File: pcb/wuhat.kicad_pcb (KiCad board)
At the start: 2 copper layers, 65 x 30 mm, 44 parts, among them J1 GPIOcon, U1 MCP3002, U3 ID

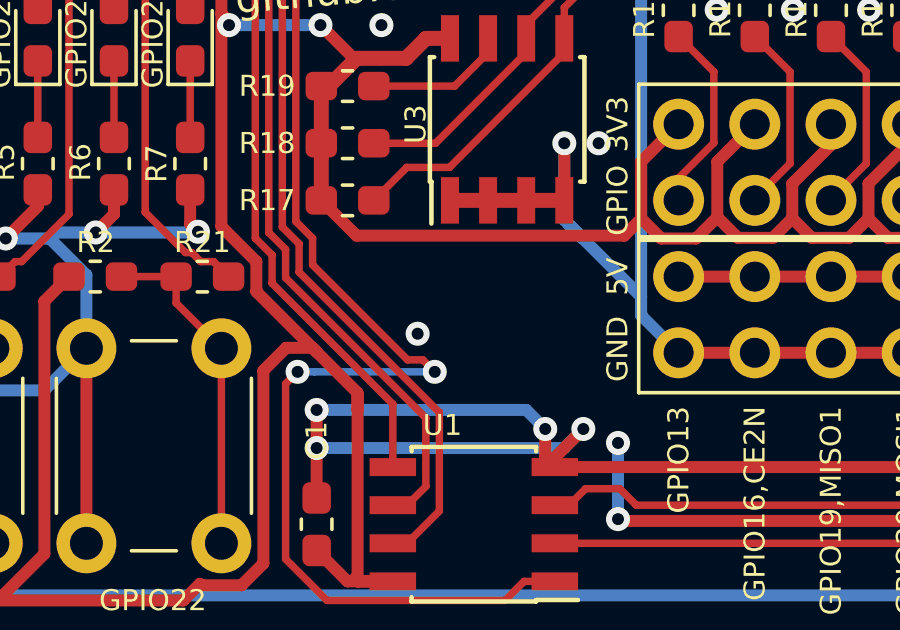
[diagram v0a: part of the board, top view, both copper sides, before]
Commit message: added revision string to pcb
bumped the revision to 7E4.0 (hex for 2020.0).
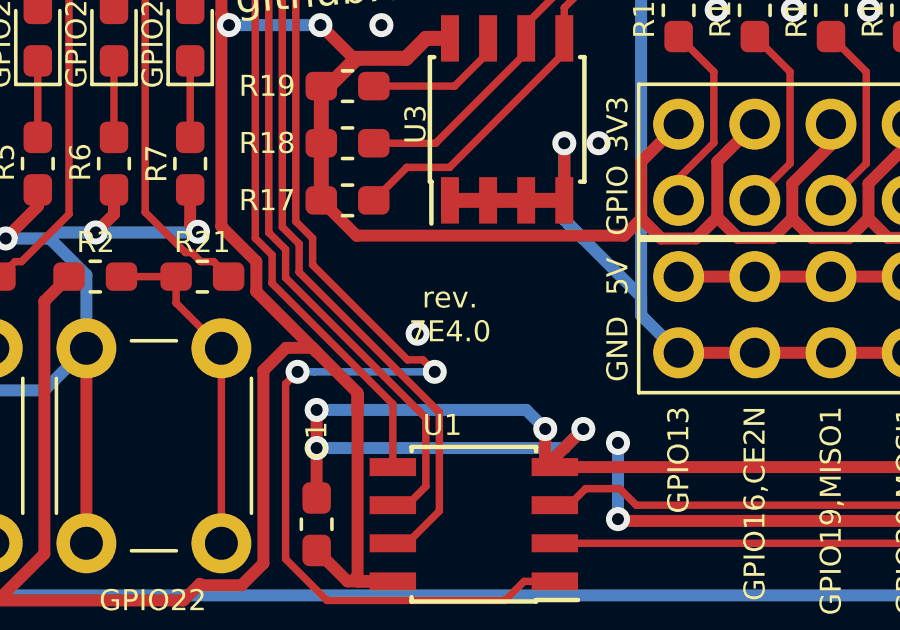
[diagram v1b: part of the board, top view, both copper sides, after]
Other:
- board text added: "rev. 7E4.0"
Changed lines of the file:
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@@
-(kicad_pcb (version 20171130) (host pcbnew 5.0.1+dfsg1-3~bpo9+1)
+(kicad_pcb (version 20171130) (host pcbnew "(5.1.4)-1")
   (general
     (thickness 1.6)
-    (drawings 43)
+    (drawings 44)
     (tracks 509)
     (zones 0)
@@
     (title WUhat)
     (date 2018-12-03)
-    (rev 0.1)
+    (rev 7E4.0)
   )
   (layers
-    (0 F.Cu signal)
-    (31 B.Cu signal)
+    (0 F.Cu signal hide)
+    (31 B.Cu signal hide)
     (32 B.Adhes user hide)
     (33 F.Adhes user hide)
@@
     (zone_45_only no)
     (trace_min 0.2)
-    (segment_width 0.15)
-    (edge_width 0.15)
     (via_size 0.8)
     (via_drill 0.4)
@@
     (uvia_min_size 0.2)
     (uvia_min_drill 0.1)
+    (edge_width 0.15)
+    (segment_width 0.15)
     (pcb_text_width 0.3)
     (pcb_text_size 1.5 1.5)
@@
     (aux_axis_origin 134.1 99.23)
     (grid_origin 134.1 99.23)
-    (visible_elements FFFFFF7F)
+    (visible_elements 7FFFFFFF)
     (pcbplotparams
       (layerselection 0x010f0_ffffffff)
@@
     (pad "" np_thru_hole circle (at 0 0) (size 6.2 6.2) (drill 2.75) (layers *.Cu *.Mask))
   )
+  (gr_text "rev.\n7E4.0" (at 137.91 114.47) (layer F.SilkS)
+    (effects (font (size 0.7 0.7) (thickness 0.15)))
+  )
   (gr_text https://github.com/wuhat (at 135.878 103.1035) (layer B.SilkS)

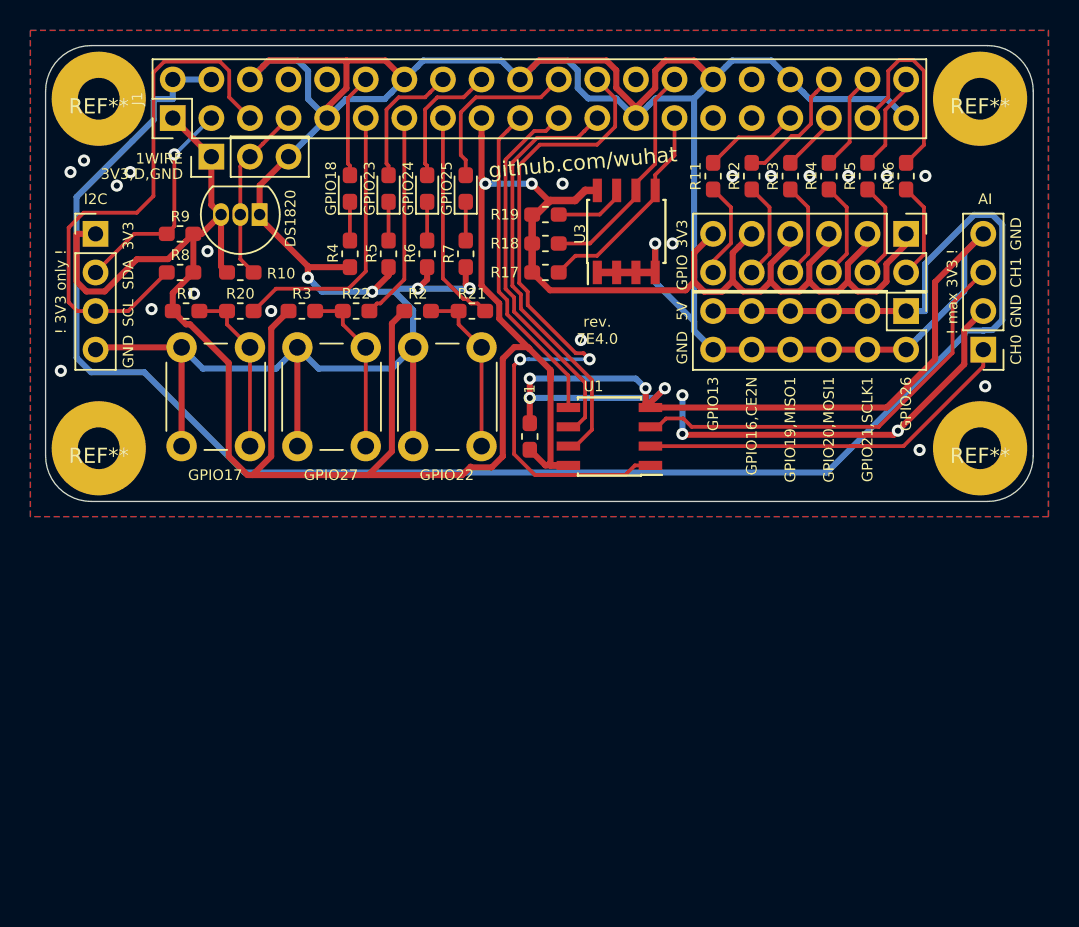
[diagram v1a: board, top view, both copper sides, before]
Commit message: expanded board to full size hat
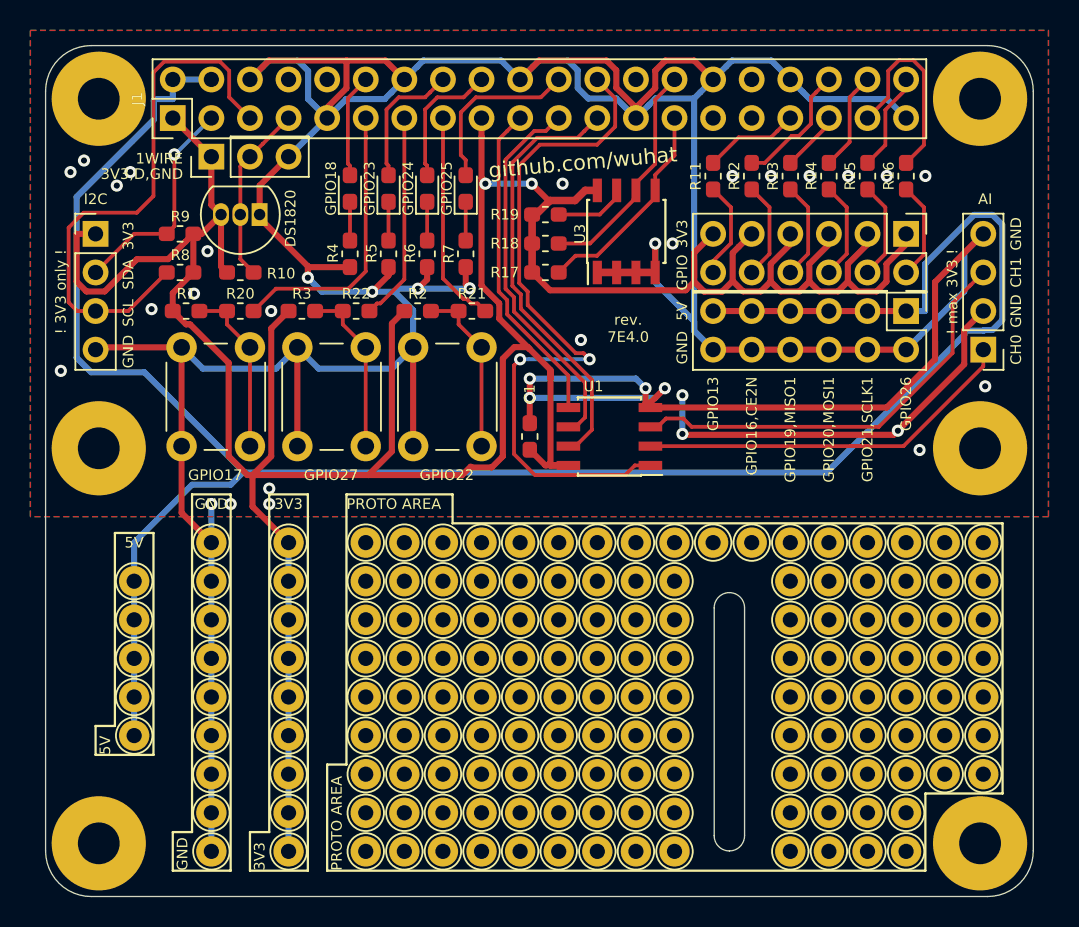
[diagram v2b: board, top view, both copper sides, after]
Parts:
- added REF**: TestPoint_THTPad_D2.0mm_Drill1.0mm, TestPoint:TestPoint_THTPad_D2.0mm_Drill1.0mm, F.Cu at (112.5, 148.8)
- added REF**: TestPoint_THTPad_D2.0mm_Drill1.0mm, TestPoint:TestPoint_THTPad_D2.0mm_Drill1.0mm, F.Cu at (117.6, 138.6)
- added REF**: TestPoint_THTPad_D2.0mm_Drill1.0mm, TestPoint:TestPoint_THTPad_D2.0mm_Drill1.0mm, F.Cu at (143.0, 146.2)
- added REF**: TestPoint_THTPad_D2.0mm_Drill1.0mm, TestPoint:TestPoint_THTPad_D2.0mm_Drill1.0mm, F.Cu at (143.0, 138.6)
- added REF**: TestPoint_THTPad_D2.0mm_Drill1.0mm, TestPoint:TestPoint_THTPad_D2.0mm_Drill1.0mm, F.Cu at (163.3, 143.7)
- added REF**: TestPoint_THTPad_D2.0mm_Drill1.0mm, TestPoint:TestPoint_THTPad_D2.0mm_Drill1.0mm, F.Cu at (160.8, 143.7)
- added REF**: TestPoint_THTPad_D2.0mm_Drill1.0mm, TestPoint:TestPoint_THTPad_D2.0mm_Drill1.0mm, F.Cu at (163.3, 138.6)
- added REF**: TestPoint_THTPad_D2.0mm_Drill1.0mm, TestPoint:TestPoint_THTPad_D2.0mm_Drill1.0mm, F.Cu at (163.3, 141.1)
- added REF**: TestPoint_THTPad_D2.0mm_Drill1.0mm, TestPoint:TestPoint_THTPad_D2.0mm_Drill1.0mm, F.Cu at (163.3, 128.4)
- added REF**: TestPoint_THTPad_D2.0mm_Drill1.0mm, TestPoint:TestPoint_THTPad_D2.0mm_Drill1.0mm, F.Cu at (163.3, 133.5)
- added REF**: TestPoint_THTPad_D2.0mm_Drill1.0mm, TestPoint:TestPoint_THTPad_D2.0mm_Drill1.0mm, F.Cu at (163.3, 136.1)
- added REF**: TestPoint_THTPad_D2.0mm_Drill1.0mm, TestPoint:TestPoint_THTPad_D2.0mm_Drill1.0mm, F.Cu at (163.3, 131.0)
- added REF**: TestPoint_THTPad_D2.0mm_Drill1.0mm, TestPoint:TestPoint_THTPad_D2.0mm_Drill1.0mm, F.Cu at (112.5, 136.1)
- added REF**: TestPoint_THTPad_D2.0mm_Drill1.0mm, TestPoint:TestPoint_THTPad_D2.0mm_Drill1.0mm, F.Cu at (160.8, 138.6)
- added REF**: TestPoint_THTPad_D2.0mm_Drill1.0mm, TestPoint:TestPoint_THTPad_D2.0mm_Drill1.0mm, F.Cu at (160.8, 141.1)
- added REF**: TestPoint_THTPad_D2.0mm_Drill1.0mm, TestPoint:TestPoint_THTPad_D2.0mm_Drill1.0mm, F.Cu at (160.8, 133.5)
- added REF**: TestPoint_THTPad_D2.0mm_Drill1.0mm, TestPoint:TestPoint_THTPad_D2.0mm_Drill1.0mm, F.Cu at (160.8, 136.1)
- added REF**: TestPoint_THTPad_D2.0mm_Drill1.0mm, TestPoint:TestPoint_THTPad_D2.0mm_Drill1.0mm, F.Cu at (160.8, 128.4)
- added REF**: TestPoint_THTPad_D2.0mm_Drill1.0mm, TestPoint:TestPoint_THTPad_D2.0mm_Drill1.0mm, F.Cu at (160.8, 131.0)
- added REF**: TestPoint_THTPad_D2.0mm_Drill1.0mm, TestPoint:TestPoint_THTPad_D2.0mm_Drill1.0mm, F.Cu at (137.9, 128.4)
- added REF**: TestPoint_THTPad_D2.0mm_Drill1.0mm, TestPoint:TestPoint_THTPad_D2.0mm_Drill1.0mm, F.Cu at (140.4, 128.4)
- added REF**: TestPoint_THTPad_D2.0mm_Drill1.0mm, TestPoint:TestPoint_THTPad_D2.0mm_Drill1.0mm, F.Cu at (143.0, 128.4)
- added REF**: TestPoint_THTPad_D2.0mm_Drill1.0mm, TestPoint:TestPoint_THTPad_D2.0mm_Drill1.0mm, F.Cu at (145.5, 128.4)
- added REF**: TestPoint_THTPad_D2.0mm_Drill1.0mm, TestPoint:TestPoint_THTPad_D2.0mm_Drill1.0mm, F.Cu at (117.6, 136.1)
- added REF**: TestPoint_THTPad_D2.0mm_Drill1.0mm, TestPoint:TestPoint_THTPad_D2.0mm_Drill1.0mm, F.Cu at (153.2, 128.4)
- added REF**: TestPoint_THTPad_D2.0mm_Drill1.0mm, TestPoint:TestPoint_THTPad_D2.0mm_Drill1.0mm, F.Cu at (155.7, 128.4)
- added REF**: TestPoint_THTPad_D2.0mm_Drill1.0mm, TestPoint:TestPoint_THTPad_D2.0mm_Drill1.0mm, F.Cu at (148.1, 128.4)
- added REF**: TestPoint_THTPad_D2.0mm_Drill1.0mm, TestPoint:TestPoint_THTPad_D2.0mm_Drill1.0mm, F.Cu at (150.6, 128.4)
- added REF**: TestPoint_THTPad_D2.0mm_Drill1.0mm, TestPoint:TestPoint_THTPad_D2.0mm_Drill1.0mm, F.Cu at (150.6, 133.5)
- added REF**: TestPoint_THTPad_D2.0mm_Drill1.0mm, TestPoint:TestPoint_THTPad_D2.0mm_Drill1.0mm, F.Cu at (150.6, 143.7)
- added REF**: TestPoint_THTPad_D2.0mm_Drill1.0mm, TestPoint:TestPoint_THTPad_D2.0mm_Drill1.0mm, F.Cu at (150.6, 136.1)
- added REF**: TestPoint_THTPad_D2.0mm_Drill1.0mm, TestPoint:TestPoint_THTPad_D2.0mm_Drill1.0mm, F.Cu at (150.6, 146.2)
- added REF**: TestPoint_THTPad_D2.0mm_Drill1.0mm, TestPoint:TestPoint_THTPad_D2.0mm_Drill1.0mm, F.Cu at (150.6, 138.6)
- added REF**: TestPoint_THTPad_D2.0mm_Drill1.0mm, TestPoint:TestPoint_THTPad_D2.0mm_Drill1.0mm, F.Cu at (150.6, 148.8)
- added REF**: TestPoint_THTPad_D2.0mm_Drill1.0mm, TestPoint:TestPoint_THTPad_D2.0mm_Drill1.0mm, F.Cu at (112.5, 133.5)
- added REF**: TestPoint_THTPad_D2.0mm_Drill1.0mm, TestPoint:TestPoint_THTPad_D2.0mm_Drill1.0mm, F.Cu at (150.6, 131.0)
- added REF**: TestPoint_THTPad_D2.0mm_Drill1.0mm, TestPoint:TestPoint_THTPad_D2.0mm_Drill1.0mm, F.Cu at (150.6, 141.1)
- added REF**: TestPoint_THTPad_D2.0mm_Drill1.0mm, TestPoint:TestPoint_THTPad_D2.0mm_Drill1.0mm, F.Cu at (153.2, 146.2)
- added REF**: TestPoint_THTPad_D2.0mm_Drill1.0mm, TestPoint:TestPoint_THTPad_D2.0mm_Drill1.0mm, F.Cu at (153.2, 143.7)
- added REF**: TestPoint_THTPad_D2.0mm_Drill1.0mm, TestPoint:TestPoint_THTPad_D2.0mm_Drill1.0mm, F.Cu at (153.2, 136.1)
- added REF**: TestPoint_THTPad_D2.0mm_Drill1.0mm, TestPoint:TestPoint_THTPad_D2.0mm_Drill1.0mm, F.Cu at (153.2, 138.6)
- added REF**: TestPoint_THTPad_D2.0mm_Drill1.0mm, TestPoint:TestPoint_THTPad_D2.0mm_Drill1.0mm, F.Cu at (153.2, 131.0)
- added REF**: TestPoint_THTPad_D2.0mm_Drill1.0mm, TestPoint:TestPoint_THTPad_D2.0mm_Drill1.0mm, F.Cu at (153.2, 133.5)
- added REF**: TestPoint_THTPad_D2.0mm_Drill1.0mm, TestPoint:TestPoint_THTPad_D2.0mm_Drill1.0mm, F.Cu at (153.2, 141.1)
- added REF**: TestPoint_THTPad_D2.0mm_Drill1.0mm, TestPoint:TestPoint_THTPad_D2.0mm_Drill1.0mm, F.Cu at (153.2, 148.8)
- added REF**: TestPoint_THTPad_D2.0mm_Drill1.0mm, TestPoint:TestPoint_THTPad_D2.0mm_Drill1.0mm, F.Cu at (117.6, 133.5)
- added REF**: TestPoint_THTPad_D2.0mm_Drill1.0mm, TestPoint:TestPoint_THTPad_D2.0mm_Drill1.0mm, F.Cu at (155.7, 148.8)
- added REF**: TestPoint_THTPad_D2.0mm_Drill1.0mm, TestPoint:TestPoint_THTPad_D2.0mm_Drill1.0mm, F.Cu at (155.7, 146.2)
- added REF**: TestPoint_THTPad_D2.0mm_Drill1.0mm, TestPoint:TestPoint_THTPad_D2.0mm_Drill1.0mm, F.Cu at (155.7, 141.1)
- added REF**: TestPoint_THTPad_D2.0mm_Drill1.0mm, TestPoint:TestPoint_THTPad_D2.0mm_Drill1.0mm, F.Cu at (155.7, 143.7)
- added REF**: TestPoint_THTPad_D2.0mm_Drill1.0mm, TestPoint:TestPoint_THTPad_D2.0mm_Drill1.0mm, F.Cu at (155.7, 136.1)
- added REF**: TestPoint_THTPad_D2.0mm_Drill1.0mm, TestPoint:TestPoint_THTPad_D2.0mm_Drill1.0mm, F.Cu at (155.7, 138.6)
- added REF**: TestPoint_THTPad_D2.0mm_Drill1.0mm, TestPoint:TestPoint_THTPad_D2.0mm_Drill1.0mm, F.Cu at (155.7, 131.0)
- added REF**: TestPoint_THTPad_D2.0mm_Drill1.0mm, TestPoint:TestPoint_THTPad_D2.0mm_Drill1.0mm, F.Cu at (155.7, 133.5)
- added REF**: TestPoint_THTPad_D2.0mm_Drill1.0mm, TestPoint:TestPoint_THTPad_D2.0mm_Drill1.0mm, F.Cu at (158.2, 148.8)
- added REF**: TestPoint_THTPad_D2.0mm_Drill1.0mm, TestPoint:TestPoint_THTPad_D2.0mm_Drill1.0mm, F.Cu at (158.2, 146.2)
- added REF**: TestPoint_THTPad_D2.0mm_Drill1.0mm, TestPoint:TestPoint_THTPad_D2.0mm_Drill1.0mm, F.Cu at (117.6, 131.0)
- added REF**: TestPoint_THTPad_D2.0mm_Drill1.0mm, TestPoint:TestPoint_THTPad_D2.0mm_Drill1.0mm, F.Cu at (158.2, 143.7)
- added REF**: TestPoint_THTPad_D2.0mm_Drill1.0mm, TestPoint:TestPoint_THTPad_D2.0mm_Drill1.0mm, F.Cu at (158.2, 141.1)
- added REF**: TestPoint_THTPad_D2.0mm_Drill1.0mm, TestPoint:TestPoint_THTPad_D2.0mm_Drill1.0mm, F.Cu at (158.2, 138.6)
- added REF**: TestPoint_THTPad_D2.0mm_Drill1.0mm, TestPoint:TestPoint_THTPad_D2.0mm_Drill1.0mm, F.Cu at (158.2, 133.5)
- added REF**: TestPoint_THTPad_D2.0mm_Drill1.0mm, TestPoint:TestPoint_THTPad_D2.0mm_Drill1.0mm, F.Cu at (158.2, 136.1)
- added REF**: TestPoint_THTPad_D2.0mm_Drill1.0mm, TestPoint:TestPoint_THTPad_D2.0mm_Drill1.0mm, F.Cu at (158.2, 131.0)
- added REF**: TestPoint_THTPad_D2.0mm_Drill1.0mm, TestPoint:TestPoint_THTPad_D2.0mm_Drill1.0mm, F.Cu at (158.2, 128.4)
- added REF**: mounting_hole, WUhat Artwork:mounting_hole, F.Cu at (163.1, 148.2)
- added REF**: TestPoint_THTPad_D2.0mm_Drill1.0mm, TestPoint:TestPoint_THTPad_D2.0mm_Drill1.0mm, F.Cu at (112.5, 131.0)
- added REF**: TestPoint_THTPad_D2.0mm_Drill1.0mm, TestPoint:TestPoint_THTPad_D2.0mm_Drill1.0mm, F.Cu at (107.4, 141.1)
- added REF**: TestPoint_THTPad_D2.0mm_Drill1.0mm, TestPoint:TestPoint_THTPad_D2.0mm_Drill1.0mm, F.Cu at (107.4, 138.6)
- added REF**: TestPoint_THTPad_D2.0mm_Drill1.0mm, TestPoint:TestPoint_THTPad_D2.0mm_Drill1.0mm, F.Cu at (107.4, 136.1)
- added REF**: TestPoint_THTPad_D2.0mm_Drill1.0mm, TestPoint:TestPoint_THTPad_D2.0mm_Drill1.0mm, F.Cu at (117.6, 148.8)
- added REF**: TestPoint_THTPad_D2.0mm_Drill1.0mm, TestPoint:TestPoint_THTPad_D2.0mm_Drill1.0mm, F.Cu at (107.4, 133.5)
- added REF**: TestPoint_THTPad_D2.0mm_Drill1.0mm, TestPoint:TestPoint_THTPad_D2.0mm_Drill1.0mm, F.Cu at (135.4, 128.4)
- added REF**: TestPoint_THTPad_D2.0mm_Drill1.0mm, TestPoint:TestPoint_THTPad_D2.0mm_Drill1.0mm, F.Cu at (130.3, 128.4)
- added REF**: TestPoint_THTPad_D2.0mm_Drill1.0mm, TestPoint:TestPoint_THTPad_D2.0mm_Drill1.0mm, F.Cu at (125.2, 128.4)
- added REF**: TestPoint_THTPad_D2.0mm_Drill1.0mm, TestPoint:TestPoint_THTPad_D2.0mm_Drill1.0mm, F.Cu at (107.4, 131.0)
- added REF**: TestPoint_THTPad_D2.0mm_Drill1.0mm, TestPoint:TestPoint_THTPad_D2.0mm_Drill1.0mm, F.Cu at (117.6, 128.4)
- added REF**: TestPoint_THTPad_D2.0mm_Drill1.0mm, TestPoint:TestPoint_THTPad_D2.0mm_Drill1.0mm, F.Cu at (112.5, 128.4)
- added REF**: TestPoint_THTPad_D2.0mm_Drill1.0mm, TestPoint:TestPoint_THTPad_D2.0mm_Drill1.0mm, F.Cu at (122.7, 128.4)
- added REF**: TestPoint_THTPad_D2.0mm_Drill1.0mm, TestPoint:TestPoint_THTPad_D2.0mm_Drill1.0mm, F.Cu at (125.2, 131.0)
- added REF**: TestPoint_THTPad_D2.0mm_Drill1.0mm, TestPoint:TestPoint_THTPad_D2.0mm_Drill1.0mm, F.Cu at (122.7, 148.8)
- added REF**: TestPoint_THTPad_D2.0mm_Drill1.0mm, TestPoint:TestPoint_THTPad_D2.0mm_Drill1.0mm, F.Cu at (112.5, 146.2)
- added REF**: TestPoint_THTPad_D2.0mm_Drill1.0mm, TestPoint:TestPoint_THTPad_D2.0mm_Drill1.0mm, F.Cu at (125.2, 146.2)
- added REF**: TestPoint_THTPad_D2.0mm_Drill1.0mm, TestPoint:TestPoint_THTPad_D2.0mm_Drill1.0mm, F.Cu at (125.2, 133.5)
- added REF**: TestPoint_THTPad_D2.0mm_Drill1.0mm, TestPoint:TestPoint_THTPad_D2.0mm_Drill1.0mm, F.Cu at (125.2, 141.1)
- added REF**: TestPoint_THTPad_D2.0mm_Drill1.0mm, TestPoint:TestPoint_THTPad_D2.0mm_Drill1.0mm, F.Cu at (122.7, 146.2)
- added REF**: TestPoint_THTPad_D2.0mm_Drill1.0mm, TestPoint:TestPoint_THTPad_D2.0mm_Drill1.0mm, F.Cu at (122.7, 143.7)
- added REF**: TestPoint_THTPad_D2.0mm_Drill1.0mm, TestPoint:TestPoint_THTPad_D2.0mm_Drill1.0mm, F.Cu at (125.2, 143.7)
- added REF**: TestPoint_THTPad_D2.0mm_Drill1.0mm, TestPoint:TestPoint_THTPad_D2.0mm_Drill1.0mm, F.Cu at (125.2, 138.6)
- added REF**: TestPoint_THTPad_D2.0mm_Drill1.0mm, TestPoint:TestPoint_THTPad_D2.0mm_Drill1.0mm, F.Cu at (122.7, 131.0)
- added REF**: TestPoint_THTPad_D2.0mm_Drill1.0mm, TestPoint:TestPoint_THTPad_D2.0mm_Drill1.0mm, F.Cu at (125.2, 136.1)
- added REF**: TestPoint_THTPad_D2.0mm_Drill1.0mm, TestPoint:TestPoint_THTPad_D2.0mm_Drill1.0mm, F.Cu at (122.7, 133.5)
- added REF**: TestPoint_THTPad_D2.0mm_Drill1.0mm, TestPoint:TestPoint_THTPad_D2.0mm_Drill1.0mm, F.Cu at (117.6, 146.2)
- added REF**: TestPoint_THTPad_D2.0mm_Drill1.0mm, TestPoint:TestPoint_THTPad_D2.0mm_Drill1.0mm, F.Cu at (125.2, 148.8)
- added REF**: TestPoint_THTPad_D2.0mm_Drill1.0mm, TestPoint:TestPoint_THTPad_D2.0mm_Drill1.0mm, F.Cu at (122.7, 141.1)
- added REF**: TestPoint_THTPad_D2.0mm_Drill1.0mm, TestPoint:TestPoint_THTPad_D2.0mm_Drill1.0mm, F.Cu at (122.7, 138.6)
- added REF**: TestPoint_THTPad_D2.0mm_Drill1.0mm, TestPoint:TestPoint_THTPad_D2.0mm_Drill1.0mm, F.Cu at (122.7, 136.1)
- added REF**: TestPoint_THTPad_D2.0mm_Drill1.0mm, TestPoint:TestPoint_THTPad_D2.0mm_Drill1.0mm, F.Cu at (130.3, 136.1)
- added REF**: TestPoint_THTPad_D2.0mm_Drill1.0mm, TestPoint:TestPoint_THTPad_D2.0mm_Drill1.0mm, F.Cu at (127.8, 141.1)
- added REF**: TestPoint_THTPad_D2.0mm_Drill1.0mm, TestPoint:TestPoint_THTPad_D2.0mm_Drill1.0mm, F.Cu at (130.3, 138.6)
- added REF**: TestPoint_THTPad_D2.0mm_Drill1.0mm, TestPoint:TestPoint_THTPad_D2.0mm_Drill1.0mm, F.Cu at (127.8, 136.1)
- added REF**: TestPoint_THTPad_D2.0mm_Drill1.0mm, TestPoint:TestPoint_THTPad_D2.0mm_Drill1.0mm, F.Cu at (127.8, 133.5)
- added REF**: TestPoint_THTPad_D2.0mm_Drill1.0mm, TestPoint:TestPoint_THTPad_D2.0mm_Drill1.0mm, F.Cu at (127.8, 131.0)
- added REF**: TestPoint_THTPad_D2.0mm_Drill1.0mm, TestPoint:TestPoint_THTPad_D2.0mm_Drill1.0mm, F.Cu at (117.6, 143.7)
- added REF**: TestPoint_THTPad_D2.0mm_Drill1.0mm, TestPoint:TestPoint_THTPad_D2.0mm_Drill1.0mm, F.Cu at (130.3, 143.7)
- added REF**: TestPoint_THTPad_D2.0mm_Drill1.0mm, TestPoint:TestPoint_THTPad_D2.0mm_Drill1.0mm, F.Cu at (127.8, 143.7)
- added REF**: TestPoint_THTPad_D2.0mm_Drill1.0mm, TestPoint:TestPoint_THTPad_D2.0mm_Drill1.0mm, F.Cu at (130.3, 148.8)
- added REF**: TestPoint_THTPad_D2.0mm_Drill1.0mm, TestPoint:TestPoint_THTPad_D2.0mm_Drill1.0mm, F.Cu at (127.8, 138.6)
- added REF**: TestPoint_THTPad_D2.0mm_Drill1.0mm, TestPoint:TestPoint_THTPad_D2.0mm_Drill1.0mm, F.Cu at (130.3, 131.0)
- added REF**: TestPoint_THTPad_D2.0mm_Drill1.0mm, TestPoint:TestPoint_THTPad_D2.0mm_Drill1.0mm, F.Cu at (127.8, 148.8)
- added REF**: TestPoint_THTPad_D2.0mm_Drill1.0mm, TestPoint:TestPoint_THTPad_D2.0mm_Drill1.0mm, F.Cu at (130.3, 146.2)
- added REF**: TestPoint_THTPad_D2.0mm_Drill1.0mm, TestPoint:TestPoint_THTPad_D2.0mm_Drill1.0mm, F.Cu at (130.3, 133.5)
- added REF**: TestPoint_THTPad_D2.0mm_Drill1.0mm, TestPoint:TestPoint_THTPad_D2.0mm_Drill1.0mm, F.Cu at (130.3, 141.1)
- added REF**: TestPoint_THTPad_D2.0mm_Drill1.0mm, TestPoint:TestPoint_THTPad_D2.0mm_Drill1.0mm, F.Cu at (127.8, 146.2)
- added REF**: TestPoint_THTPad_D2.0mm_Drill1.0mm, TestPoint:TestPoint_THTPad_D2.0mm_Drill1.0mm, F.Cu at (112.5, 143.7)
- added REF**: TestPoint_THTPad_D2.0mm_Drill1.0mm, TestPoint:TestPoint_THTPad_D2.0mm_Drill1.0mm, F.Cu at (127.8, 128.4)
- added REF**: TestPoint_THTPad_D2.0mm_Drill1.0mm, TestPoint:TestPoint_THTPad_D2.0mm_Drill1.0mm, F.Cu at (135.4, 133.5)
- added REF**: TestPoint_THTPad_D2.0mm_Drill1.0mm, TestPoint:TestPoint_THTPad_D2.0mm_Drill1.0mm, F.Cu at (132.8, 133.5)
- added REF**: TestPoint_THTPad_D2.0mm_Drill1.0mm, TestPoint:TestPoint_THTPad_D2.0mm_Drill1.0mm, F.Cu at (135.4, 141.1)
- added REF**: TestPoint_THTPad_D2.0mm_Drill1.0mm, TestPoint:TestPoint_THTPad_D2.0mm_Drill1.0mm, F.Cu at (135.4, 148.8)
- added REF**: TestPoint_THTPad_D2.0mm_Drill1.0mm, TestPoint:TestPoint_THTPad_D2.0mm_Drill1.0mm, F.Cu at (132.8, 141.1)
- added REF**: TestPoint_THTPad_D2.0mm_Drill1.0mm, TestPoint:TestPoint_THTPad_D2.0mm_Drill1.0mm, F.Cu at (135.4, 138.6)
- added REF**: TestPoint_THTPad_D2.0mm_Drill1.0mm, TestPoint:TestPoint_THTPad_D2.0mm_Drill1.0mm, F.Cu at (135.4, 136.1)
- added REF**: TestPoint_THTPad_D2.0mm_Drill1.0mm, TestPoint:TestPoint_THTPad_D2.0mm_Drill1.0mm, F.Cu at (135.4, 131.0)
- added REF**: TestPoint_THTPad_D2.0mm_Drill1.0mm, TestPoint:TestPoint_THTPad_D2.0mm_Drill1.0mm, F.Cu at (132.8, 148.8)
- added REF**: TestPoint_THTPad_D2.0mm_Drill1.0mm, TestPoint:TestPoint_THTPad_D2.0mm_Drill1.0mm, F.Cu at (112.5, 141.1)
- added REF**: TestPoint_THTPad_D2.0mm_Drill1.0mm, TestPoint:TestPoint_THTPad_D2.0mm_Drill1.0mm, F.Cu at (132.8, 138.6)
- added REF**: TestPoint_THTPad_D2.0mm_Drill1.0mm, TestPoint:TestPoint_THTPad_D2.0mm_Drill1.0mm, F.Cu at (135.4, 143.7)
- added REF**: TestPoint_THTPad_D2.0mm_Drill1.0mm, TestPoint:TestPoint_THTPad_D2.0mm_Drill1.0mm, F.Cu at (132.8, 136.1)
- added REF**: TestPoint_THTPad_D2.0mm_Drill1.0mm, TestPoint:TestPoint_THTPad_D2.0mm_Drill1.0mm, F.Cu at (132.8, 131.0)
- added REF**: TestPoint_THTPad_D2.0mm_Drill1.0mm, TestPoint:TestPoint_THTPad_D2.0mm_Drill1.0mm, F.Cu at (132.8, 143.7)
- added REF**: TestPoint_THTPad_D2.0mm_Drill1.0mm, TestPoint:TestPoint_THTPad_D2.0mm_Drill1.0mm, F.Cu at (135.4, 146.2)
- added REF**: TestPoint_THTPad_D2.0mm_Drill1.0mm, TestPoint:TestPoint_THTPad_D2.0mm_Drill1.0mm, F.Cu at (132.8, 146.2)
- added REF**: TestPoint_THTPad_D2.0mm_Drill1.0mm, TestPoint:TestPoint_THTPad_D2.0mm_Drill1.0mm, F.Cu at (132.8, 128.4)
- added REF**: TestPoint_THTPad_D2.0mm_Drill1.0mm, TestPoint:TestPoint_THTPad_D2.0mm_Drill1.0mm, F.Cu at (143.0, 148.8)
- added REF**: TestPoint_THTPad_D2.0mm_Drill1.0mm, TestPoint:TestPoint_THTPad_D2.0mm_Drill1.0mm, F.Cu at (140.4, 148.8)
- added REF**: TestPoint_THTPad_D2.0mm_Drill1.0mm, TestPoint:TestPoint_THTPad_D2.0mm_Drill1.0mm, F.Cu at (117.6, 141.1)
- added REF**: TestPoint_THTPad_D2.0mm_Drill1.0mm, TestPoint:TestPoint_THTPad_D2.0mm_Drill1.0mm, F.Cu at (137.9, 148.8)
- added REF**: TestPoint_THTPad_D2.0mm_Drill1.0mm, TestPoint:TestPoint_THTPad_D2.0mm_Drill1.0mm, F.Cu at (137.9, 133.5)
- added REF**: TestPoint_THTPad_D2.0mm_Drill1.0mm, TestPoint:TestPoint_THTPad_D2.0mm_Drill1.0mm, F.Cu at (137.9, 141.1)
- added REF**: TestPoint_THTPad_D2.0mm_Drill1.0mm, TestPoint:TestPoint_THTPad_D2.0mm_Drill1.0mm, F.Cu at (137.9, 138.6)
- added REF**: TestPoint_THTPad_D2.0mm_Drill1.0mm, TestPoint:TestPoint_THTPad_D2.0mm_Drill1.0mm, F.Cu at (137.9, 136.1)
- added REF**: TestPoint_THTPad_D2.0mm_Drill1.0mm, TestPoint:TestPoint_THTPad_D2.0mm_Drill1.0mm, F.Cu at (137.9, 131.0)
- added REF**: TestPoint_THTPad_D2.0mm_Drill1.0mm, TestPoint:TestPoint_THTPad_D2.0mm_Drill1.0mm, F.Cu at (137.9, 143.7)
- added REF**: TestPoint_THTPad_D2.0mm_Drill1.0mm, TestPoint:TestPoint_THTPad_D2.0mm_Drill1.0mm, F.Cu at (137.9, 146.2)
- added REF**: TestPoint_THTPad_D2.0mm_Drill1.0mm, TestPoint:TestPoint_THTPad_D2.0mm_Drill1.0mm, F.Cu at (140.4, 138.6)
- added REF**: TestPoint_THTPad_D2.0mm_Drill1.0mm, TestPoint:TestPoint_THTPad_D2.0mm_Drill1.0mm, F.Cu at (140.4, 136.1)
- added REF**: TestPoint_THTPad_D2.0mm_Drill1.0mm, TestPoint:TestPoint_THTPad_D2.0mm_Drill1.0mm, F.Cu at (112.5, 138.6)
- added REF**: TestPoint_THTPad_D2.0mm_Drill1.0mm, TestPoint:TestPoint_THTPad_D2.0mm_Drill1.0mm, F.Cu at (140.4, 133.5)
- added REF**: TestPoint_THTPad_D2.0mm_Drill1.0mm, TestPoint:TestPoint_THTPad_D2.0mm_Drill1.0mm, F.Cu at (140.4, 146.2)
- added REF**: TestPoint_THTPad_D2.0mm_Drill1.0mm, TestPoint:TestPoint_THTPad_D2.0mm_Drill1.0mm, F.Cu at (140.4, 143.7)
- added REF**: TestPoint_THTPad_D2.0mm_Drill1.0mm, TestPoint:TestPoint_THTPad_D2.0mm_Drill1.0mm, F.Cu at (140.4, 131.0)
- added REF**: TestPoint_THTPad_D2.0mm_Drill1.0mm, TestPoint:TestPoint_THTPad_D2.0mm_Drill1.0mm, F.Cu at (140.4, 141.1)
- added REF**: TestPoint_THTPad_D2.0mm_Drill1.0mm, TestPoint:TestPoint_THTPad_D2.0mm_Drill1.0mm, F.Cu at (143.0, 136.1)
- added REF**: TestPoint_THTPad_D2.0mm_Drill1.0mm, TestPoint:TestPoint_THTPad_D2.0mm_Drill1.0mm, F.Cu at (143.0, 141.1)
- added REF**: TestPoint_THTPad_D2.0mm_Drill1.0mm, TestPoint:TestPoint_THTPad_D2.0mm_Drill1.0mm, F.Cu at (143.0, 143.7)
- added REF**: TestPoint_THTPad_D2.0mm_Drill1.0mm, TestPoint:TestPoint_THTPad_D2.0mm_Drill1.0mm, F.Cu at (143.0, 133.5)
- added REF**: TestPoint_THTPad_D2.0mm_Drill1.0mm, TestPoint:TestPoint_THTPad_D2.0mm_Drill1.0mm, F.Cu at (143.0, 131.0)
- added e: mounting_hole, WUhat Artwork:mounting_hole, F.Cu at (105.1, 122.2)
- moved e 26.0 mm to (105.1, 148.2)
- renumbered REF** to e
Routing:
- net GND: track 301.7 -> 331.7 mm, vias 32 -> 36
- net +3V3: track 190.0 -> 215.7 mm
- net +5V: track 122.5 -> 144.4 mm
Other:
- board size 65 x 30 mm -> 65 x 56 mm
- board text added: "PROTO AREA"
